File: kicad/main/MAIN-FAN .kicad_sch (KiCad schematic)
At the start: 8 parts, among them Q1 2302V

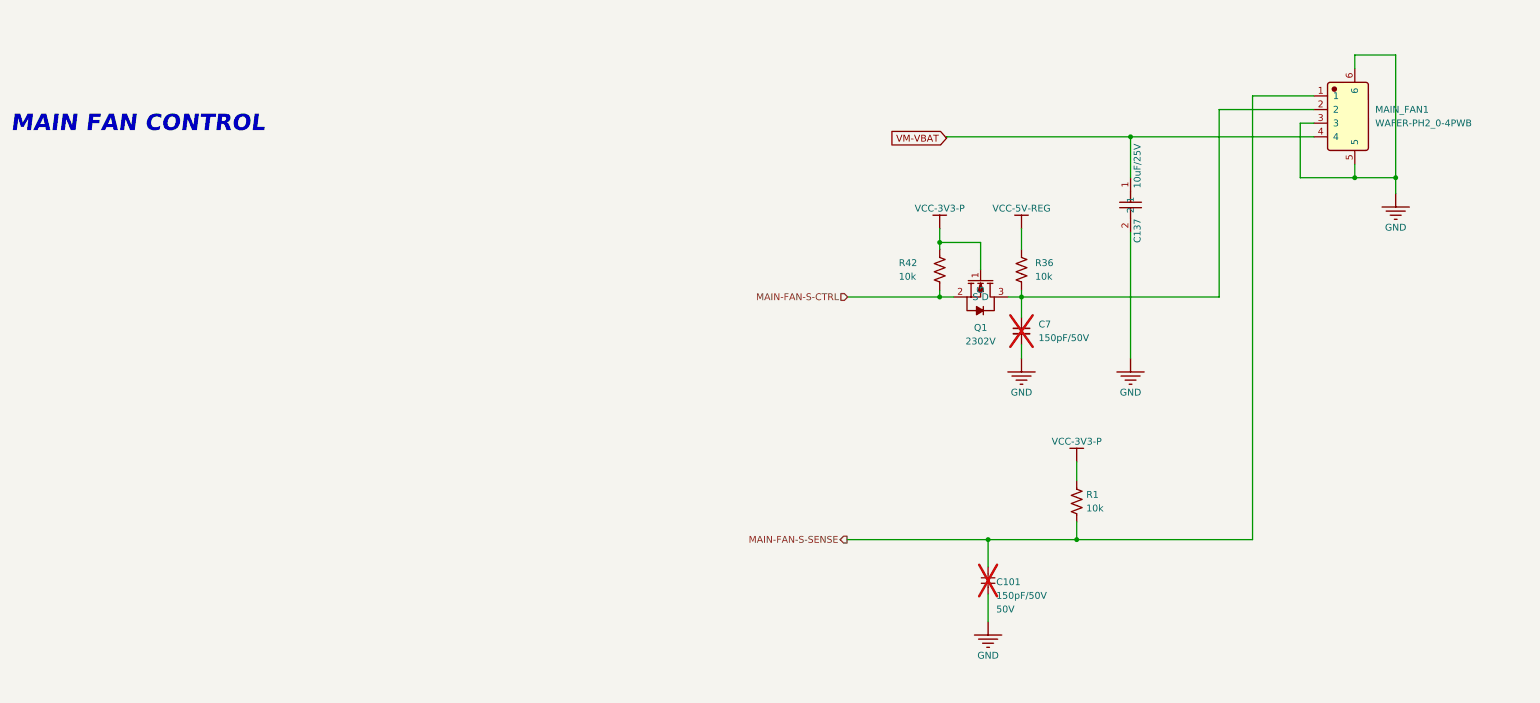
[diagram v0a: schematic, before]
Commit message: Cliff/bumpers connector
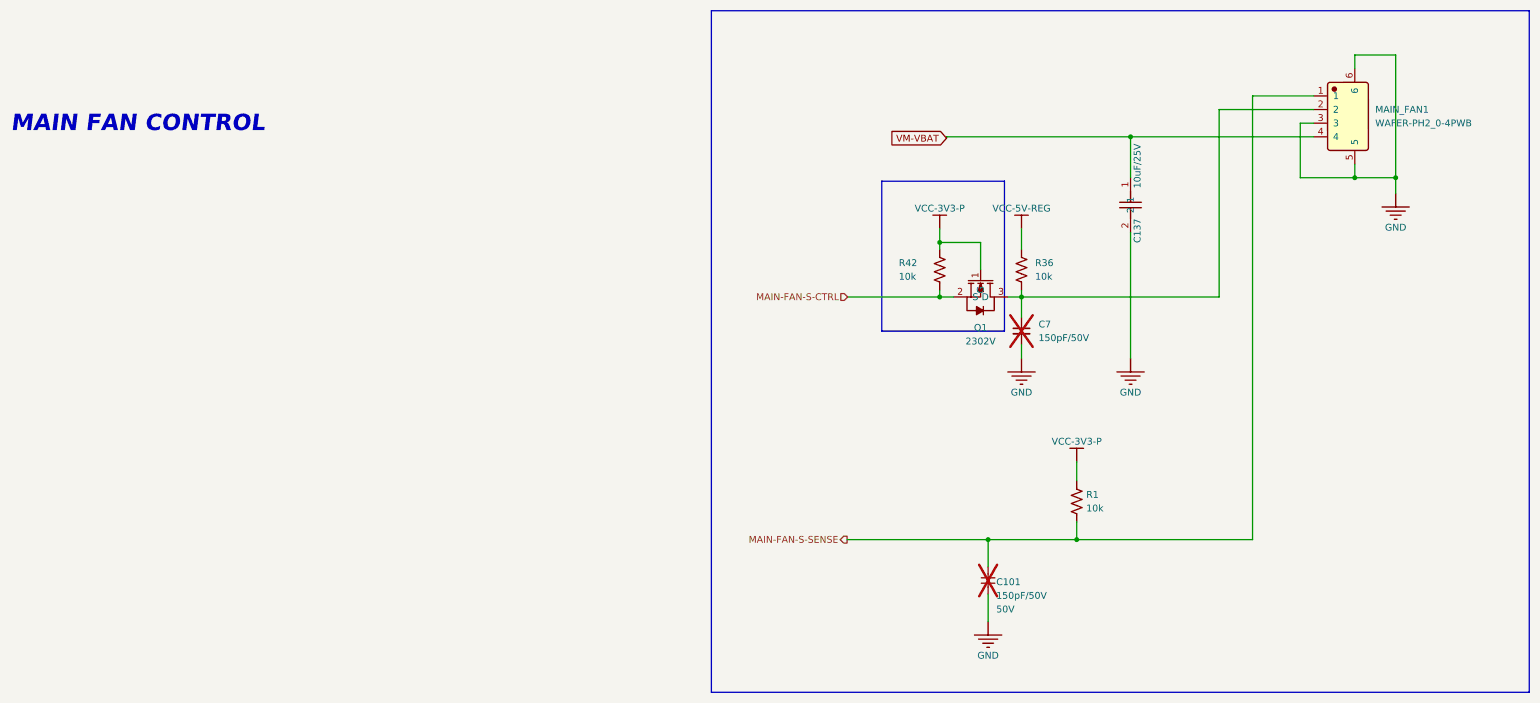
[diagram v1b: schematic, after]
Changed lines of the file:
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@@
 	(generator_version "10.0")
 	(paper "A2")
+	(rectangle
+		(start 308.61 106.68)
+		(end 461.01 233.68)
+		(stroke
+			(width 0)
+			(type solid)
+		)
+		(fill
+			(type color)
+			(color 0 72 0 1)
+		)
+	)
+	(rectangle
+		(start 340.36 138.43)
+		(end 363.22 166.37)
+		(stroke
+			(width 0)
+			(type solid)
+		)
+		(fill
+			(type color)
+			(color 132 0 0 1)
+		)
+	)
 	(text "MAIN FAN CONTROL"
 		(exclude_from_sim no)

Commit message: Second review round
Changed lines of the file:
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@@
 	(generator_version "10.0")
 	(paper "A2")
-	(rectangle
-		(start 308.61 106.68)
-		(end 461.01 233.68)
-		(stroke
-			(width 0)
-			(type solid)
-		)
-		(fill
-			(type color)
-			(color 0 72 0 1)
-		)
-	)
-	(rectangle
-		(start 340.36 138.43)
-		(end 363.22 166.37)
-		(stroke
-			(width 0)
-			(type solid)
-		)
-		(fill
-			(type color)
-			(color 132 0 0 1)
-		)
-	)
 	(text "MAIN FAN CONTROL"
 		(exclude_from_sim no)

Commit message: STM32 power rail switch
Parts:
- removed Q1: 2302V, JLCImport:2302V, symbol JLCImport:2302V
- removed R36, R42: 10k, Resistor_SMD:R_0603_1608Metric, symbol Device:R_US
- added R74: 100k, Resistor_SMD:R_0603_1608Metric, symbol Device:R_US
- C101: LCSC (none) -> C107075; VOLTAGERATE 50V -> (none)
- C7: LCSC (none) -> C107075
- R1: LCSC (none) -> C98220
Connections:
- net GND: now also R74.2
- net MAIN-FAN-S-CTRL: now also C7.1, MAIN_FAN1.2, R74.1
- net VCC-3V3-P renamed VCC-3V3-REG
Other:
- moved on the sheet: C101, C7, R1
